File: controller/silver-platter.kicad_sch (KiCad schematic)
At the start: 25 parts, among them J1 UART, J2 JTAG/SWJ, J3 Solder Pad, SW1 SW_Push, SW2 SPDT, U1 STM32F205RETx

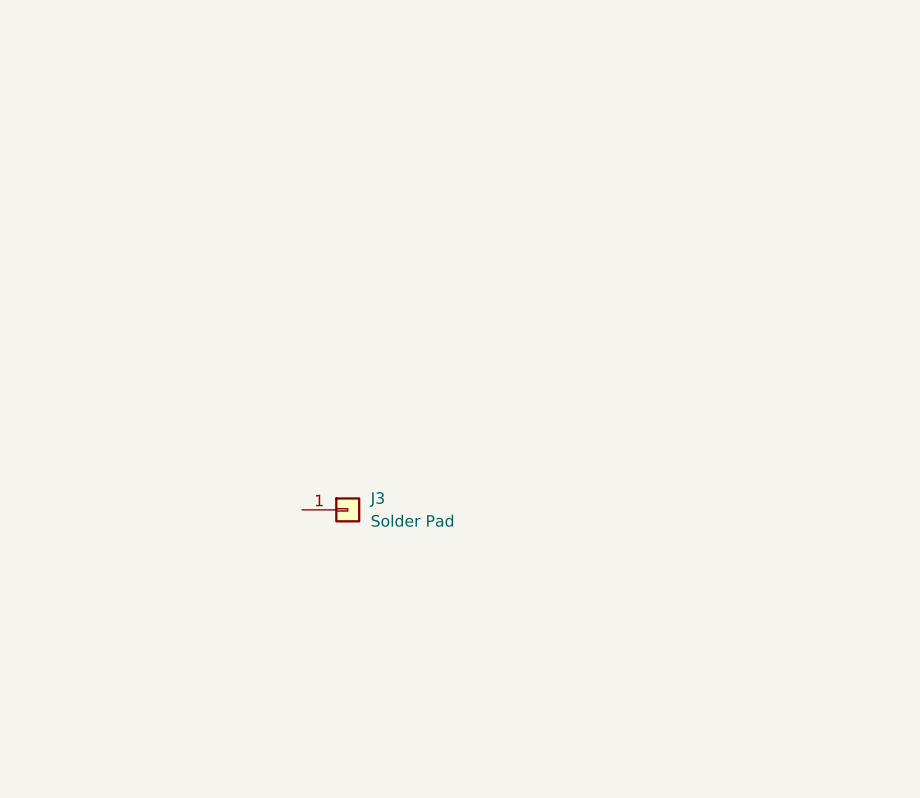
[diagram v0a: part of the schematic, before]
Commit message: LED drive circuit added to schematic
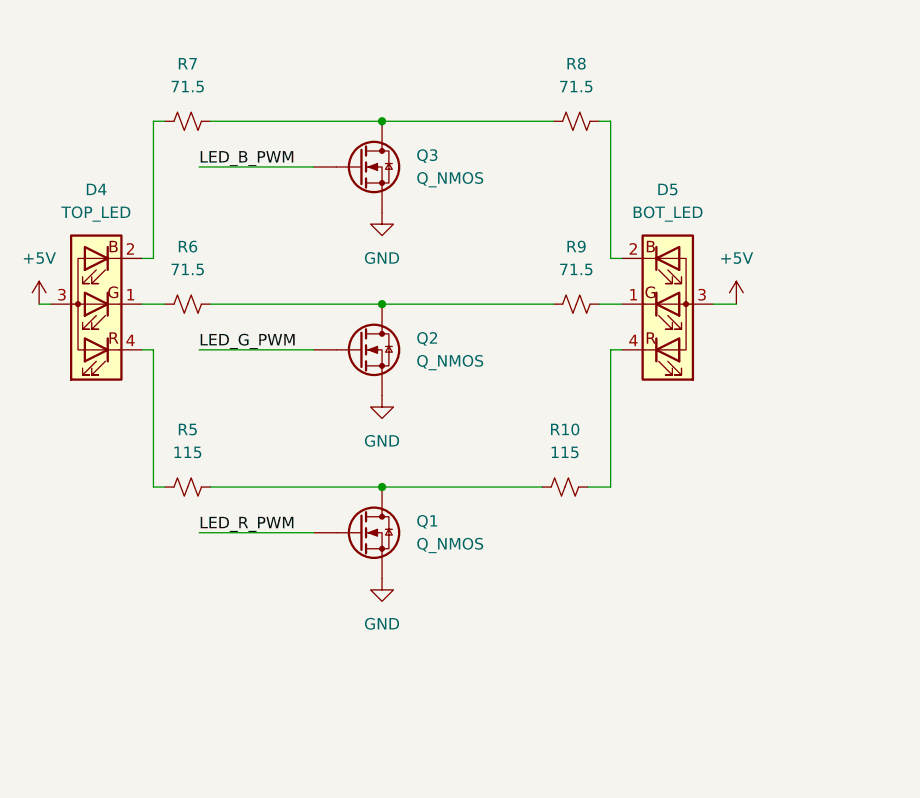
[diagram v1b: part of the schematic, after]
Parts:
- removed J3: Solder Pad, symbol Connector_Generic:Conn_01x01
- added D4: TOP_LED, symbol Device:LED_GBAR
- added D5: BOT_LED, symbol Device:LED_GBAR
- added Q1, Q2, Q3: Q_NMOS, symbol Device:Q_NMOS
- added R10, R5: 115, symbol Device:R_Small_US
- added R6, R7, R8, R9: 71.5, symbol Device:R_Small_US
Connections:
- net GND: now also Q1.S, Q2.S, Q3.S
- net LED_B_PWM: now also Q3.G
- net LED_G_PWM: now also Q2.G
- net LED_R_PWM: now also Q1.G
- new net: D5.4 (RK), R10.1
- new net: Q1.D, R10.2, R5.1
- new net: Q3.D, R7.1, R8.2
- new net: D5.2 (BK), R8.1
- new net: D5.1 (GK), R9.1
- new net: D4.4 (RK), R5.2
- new net: D4.1 (GK), R6.2
- new net: D4.2 (BK), R7.2
- new net: Q2.D, R6.1, R9.2
- new net +5V: D4.3 (A), D5.3 (A)

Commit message: Schematic Draft 1
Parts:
- removed D4: TOP_LED, symbol Device:LED_GBAR
- removed D5: BOT_LED, symbol Device:LED_GBAR
- removed SW2: SPDT, symbol Switch:SW_SPDT
- added C13, C14, C15: 2.2u, Capacitor_SMD:C_0603_1608Metric_Pad1.08x0.95mm_HandSolder, symbol Device:C_Small
- added C16: 100n, Capacitor_SMD:C_0603_1608Metric_Pad1.08x0.95mm_HandSolder, symbol Device:C_Small
- added C17: 10u, Capacitor_SMD:C_0603_1608Metric_Pad1.08x0.95mm_HandSolder, symbol Device:C_Small
- added J10: GND_ESC, TestPoint:TestPoint_Pad_4.0x4.0mm, symbol Connector_Generic:Conn_01x01
- added J11: LED1_B, TestPoint:TestPoint_Pad_4.0x4.0mm, symbol Connector_Generic:Conn_01x01
- added J12: LED1_G, TestPoint:TestPoint_Pad_4.0x4.0mm, symbol Connector_Generic:Conn_01x01
- added J13: LED1_R, TestPoint:TestPoint_Pad_4.0x4.0mm, symbol Connector_Generic:Conn_01x01
- added J14: LED1_ANODE, TestPoint:TestPoint_Pad_4.0x4.0mm, symbol Connector_Generic:Conn_01x01
- added J15: LED2_B, TestPoint:TestPoint_Pad_4.0x4.0mm, symbol Connector_Generic:Conn_01x01
- added J16: LED2_G, TestPoint:TestPoint_Pad_4.0x4.0mm, symbol Connector_Generic:Conn_01x01
- added J17: LED2_R, TestPoint:TestPoint_Pad_4.0x4.0mm, symbol Connector_Generic:Conn_01x01
- added J18: LED2_ANODE, TestPoint:TestPoint_Pad_4.0x4.0mm, symbol Connector_Generic:Conn_01x01
- added J19: RX_VDD, TestPoint:TestPoint_Pad_4.0x4.0mm, symbol Connector_Generic:Conn_01x01
- added J20: RX_iBUS, TestPoint:TestPoint_Pad_4.0x4.0mm, symbol Connector_Generic:Conn_01x01
- added J21: RX_GND, TestPoint:TestPoint_Pad_4.0x4.0mm, symbol Connector_Generic:Conn_01x01
- added J22: BOOT, Connector_PinHeader_2.54mm:PinHeader_1x02_P2.54mm_Vertical, symbol Connector_Generic:Conn_01x02
- added J23: +BATT, TestPoint:TestPoint_Pad_4.0x4.0mm, symbol Connector_Generic:Conn_01x01
- added J24: -BATT, TestPoint:TestPoint_Pad_4.0x4.0mm, symbol Connector_Generic:Conn_01x01
- added J3: VDD_ACCEL, TestPoint:TestPoint_Pad_4.0x4.0mm, symbol Connector_Generic:Conn_01x01
- added J4: SCL_ACCEL, TestPoint:TestPoint_Pad_4.0x4.0mm, symbol Connector_Generic:Conn_01x01
- added J5: SDA_ACCEL, TestPoint:TestPoint_Pad_4.0x4.0mm, symbol Connector_Generic:Conn_01x01
- added J6: GND_ACCEL, TestPoint:TestPoint_Pad_4.0x4.0mm, symbol Connector_Generic:Conn_01x01
- added J7: VBAT_ESC, TestPoint:TestPoint_Pad_4.0x4.0mm, symbol Connector_Generic:Conn_01x01
- added J8: CH1_ESC, TestPoint:TestPoint_Pad_4.0x4.0mm, symbol Connector_Generic:Conn_01x01
- added J9: CH2_ESC, TestPoint:TestPoint_Pad_4.0x4.0mm, symbol Connector_Generic:Conn_01x01
- added L1: 4.7u, Inductor_SMD:L_1008_2520Metric_Pad1.43x2.20mm_HandSolder, symbol Device:L_Small
- added R11: 4.3k, Resistor_SMD:R_0603_1608Metric_Pad0.98x0.95mm_HandSolder, symbol Device:R_Small_US
- added R12: 1.1k, Resistor_SMD:R_0603_1608Metric_Pad0.98x0.95mm_HandSolder, symbol Device:R_Small_US
- added TP1: +5V, TestPoint:TestPoint_Plated_Hole_D2.0mm, symbol Connector:TestPoint
- added TP2: +3V3, TestPoint:TestPoint_Plated_Hole_D2.0mm, symbol Connector:TestPoint
- added TP3: +BATT, TestPoint:TestPoint_Plated_Hole_D2.0mm, symbol Connector:TestPoint
- added U2: TLV74033PDBVR, Package_TO_SOT_SMD:SOT-23-5, symbol Regulator_Linear:TLV74033PDBVR
- added U3: LMR50410Y5FQDBVRQ1, Package_TO_SOT_SMD:SOT-23-6_Handsoldering, symbol Regulator_Switching:LMR50410Y5FQDBVRQ1
- C1, C10, C12, C2, C3, C4, C5, C6, C7, C8, C9: footprint (none) -> Capacitor_SMD:C_0603_1608Metric_Pad1.08x0.95mm_HandSolder
- D1, D2, D3: footprint (none) -> Diode_SMD:D_0603_1608Metric_Pad1.05x0.95mm_HandSolder
- FB1: footprint (none) -> Inductor_SMD:L_0603_1608Metric_Pad1.05x0.95mm_HandSolder
- J1: footprint (none) -> Connector_PinHeader_2.54mm:PinHeader_1x04_P2.54mm_Vertical
- J2: footprint (none) -> Connector_Wuerth:Wuerth_WR-BHD_61202021621_P2.54mm_Vertical
- Q1, Q2, Q3: footprint (none) -> Package_TO_SOT_SMD:SOT-23
- R1, R10, R5, R6, R7, R8, R9: footprint (none) -> Resistor_SMD:R_0603_1608Metric_Pad0.98x0.95mm_HandSolder
- R2, R3, R4: value 1k -> 1.1k; footprint (none) -> Resistor_SMD:R_0603_1608Metric_Pad0.98x0.95mm_HandSolder
- SW1: footprint (none) -> Button_Switch_THT:SW_PUSH_6mm
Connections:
- net +5V: now also C13.1, C17.1, J14.1 (Pin_1), J18.1 (Pin_1), J19.1 (Pin_1), L1.2, TP1.1, U2.1 (IN), U2.3 (EN), U3.3 (FB)
- net BOOT: now also J22.1 (Pin_1)
- net DSHOT_CH1: now also J8.1 (Pin_1)
- net DSHOT_CH2: now also J9.1 (Pin_1)
- net GND: now also R1.1, C13.2, C14.2, C15.2, C17.2, J10.1 (Pin_1), J21.1 (Pin_1), J24.1 (Pin_1), J6.1 (Pin_1), R12.1, U2.2 (GND), U3.2 (GND)
- net I2C2_SCL: now also J4.1 (Pin_1)
- net I2C2_SDA: now also J5.1 (Pin_1)
- net iBUS: now also J20.1 (Pin_1)
- net at R10.1: now also J13.1 (Pin_1)
- net at R8.1: now also J11.1 (Pin_1)
- net at R9.1: now also J12.1 (Pin_1)
- net at R5.2: now also J17.1 (Pin_1)
- net at R6.2: now also J16.1 (Pin_1)
- net at R7.2: now also J15.1 (Pin_1)
- net VBAT: no longer names the net of U1.15 (PA1)
- net VBAT: now also R11.1, R12.2
- net VDD renamed +3V3
- net +3V3: now also C14.1, J22.2 (Pin_2), J3.1 (Pin_1), TP2.1, U2.5 (OUT)
- new net: C16.2, L1.1, U3.6 (SW)
- new net: C16.1, U3.1 (CB)
- new net +BATT: C15.1, J23.1 (Pin_1), J7.1 (Pin_1), R11.2, TP3.1, U3.4 (EN), U3.5 (VIN)
- no-connect marks 3 -> 39
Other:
- moved on the sheet: C1, C2, C3, C4, C5, C6, C7, C8, D1, FB1, Q1, Q2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
